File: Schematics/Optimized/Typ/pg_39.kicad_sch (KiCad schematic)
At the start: 35 parts, among them U4101 F374, U4102 F00, U4103 F04, U4104 F30, U4105 F51, U4109 F37, U4110 F02, U4111 F64, U4112 F64, U4113 F02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

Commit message: TYP+VAL condensation
Tested: passed expmon_test_val (-muxbus)
Tested: passed expmon_test_typ (-muxbus)
Tested: passed run_udiag
Tested: passed boot_env (R2_INTEG until PRETTY_PRINTER)
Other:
- moved on the sheet: GB226, GB274, GB275, GB276, GB277, GB278, GB281, GB282, GB283, GB284, U4104, U4105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

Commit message: Integrate R2_TV (mainly state clock)
Tested: passed run_udiag
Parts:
- removed U4105: F51, symbol r1000:F51
- removed U4109, U4124, U4125, U4126: F37, symbol r1000:F37
- removed U4119: F00, symbol r1000:F00
- removed U4121, U4122, U4123: F02, symbol r1000:F02
- added GB301, GB302, GB303, GB304, GB305, GB308, GB309, GB310, GB311, GB312, GB313, GB314: GB, symbol r1000:GB
- added U2117: XTVSCLK, symbol r1000:XTVSCLK
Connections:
- net ARF_WE.EN~: now also U2117.23 (ARFWR)
- net BRF_WE.EN~: now also U2117.26 (BRFWR)
- net CLK.2XE~: now also GB302.1
- net COND_CLK.EN~: now also U2117.11 (CCE)
- net COND~.SCLK: now also U2117.4 (CCLK)
- net CSA.DIAG.EN~: now also U2117.13 (ACE)
- net CSA~.SCLK: now also U2117.6 (ACLK)
- net H1: now also GB309.1
- net H2: now also GB310.1, U2117.3 (H2)
- net H2E: now also GB308.1
- net OF_CLK.EN~: now also U2117.9 (ZCE)
- net OF~.SCLK: now also U2117.2 (ZCLK)
- net Q2~: now also GB312.1
- net Q3~: now also GB313.1, U2117.5 (Q3)
- net RAM_STOP~: now also U2117.20 (RMS)
- net SF_STOP: now also U2117.18 (SFS)
- net STATE_CLK.EN~: now also U2117.7 (SCE)
- net STATE_STOP~: now also U2117.19 (STS)
- net UIR.DIAG_OFF: now also U2117.17 (UOF)
- net UIR.DIAG_ON~: now also U2117.15 (UON)
- net UIR~.SCLK: now also U2117.8 (UCLK)
- net WE.EN~: now also U2117.22 (WEEN)
- net WEL: now reaches U4117.5 (D3), U4118.5 (Q)
- net WEL: now also U2117.21 (WEL)
- new net ACS.DIAG_OFF~: U2117.24 (ACOFF)
- new net A_L.DIAG_OFF~: U2117.25 (ALOFF)
- new net A_RF.CS~: U2117.10 (ARFCS)
- new net A_RF.WE~: U2117.12 (ARFWE)
- new net BCS.DIAG_OFF~: U2117.27 (BCOFF)
- new net B_L.DIAG_OFF~: U2117.28 (BLOFF)
- new net B_RF.CS~: U2117.14 (BRFCS)
- new net B_RF.WE~: U2117.16 (BRFWE)
- new net CLK.2X: GB303.1
- new net CLK.2XE: GB301.1, U2117.1 (2XE)
- new net CLK.2X~: GB304.1
- new net H1.PHD: GB305.1
- new net Q1~: GB311.1
- new net Q4~: GB314.1
- no-connect marks 13 -> 11
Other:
- moved on the sheet: GB226, GB274, GB275, GB276, GB277, GB278, GB281, GB282, GB283, GB284, GB285, GB291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

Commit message: XCLKSTP, XIOP XSUDEC
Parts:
- removed GB308: GB, symbol r1000:GB
- removed U4102: F00, symbol r1000:F00
- removed U4103, U4114, U4115, U4116: F04, symbol r1000:F04
- removed U4104: F30, symbol r1000:F30
- removed U4110, U4113: F02, symbol r1000:F02
- removed U4111, U4112: F64, symbol r1000:F64
- added U901: F04, symbol r1000:F04
- added U903: XCLKSTPTV, symbol r1000:XCLKSTPTV
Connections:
- net WE.EN~ is gone; now on net DIAG_STOP: U2117.22 (DSTOP)
- net DIAG.NO_STOP: now also U903.3 (DFCLK)
- net DIAG_STOP: now also U4118.2 (D)
- net FREEZE: now also U903.6 (FREEZ)
- net Q3~: now also U903.1 (Q3)
- net Q4~: now also U901.1 (D0)
- net RAM_STOP~: now also U903.8 (RAMRUN)
- net SF_STOP: now also U903.4 (SFSTP)
- net STATE_STOP~: now also U903.2 (CLKRUN)
- net T.BHMAC_STOP~: now also U903.18 (STOP7)
- net T.DIAG_FREEZE~: now also U903.7 (DIAG1); no longer U4101.14 (D5)
- net T.DIAG_SYNC~: now also U903.5 (DIAG0); no longer U4101.13 (D4)
- net T.ECC_STOP: now also U903.9 (ECC0)
- net T.ECC_STOP.EN: now also U903.10 (ECC1)
- net T.FIELD_STOP~: now also U903.16 (STOP5)
- net T.MEM_STOP~: now also U903.11 (STOP0)
- net T.MICRO_STOP~: now also U903.17 (STOP6)
- net T.SPARE_STOP~: now also U903.13 (STOP2)
- net T.SYS_STOP~: now also U903.12 (STOP1)
- net T.TYPE0_STOP~: now also U903.14 (STOP3)
- net T.TYPE1_STOP~: now also U903.15 (STOP4)
- net WEL: now also U4118.6 (Q_); no longer U4118.5 (Q)
- net H2E: no longer names the net of U4117.1 (D0)
- net H2E: now also U901.2 (Q)
- new net CSA_WRITE_EN: U903.19 (CSAWR)
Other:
- moved on the sheet: GB226, GB274, GB275, GB276, GB277, GB278, GB281, GB282, GB283, GB284, GB285, GB291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

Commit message: Lots of work
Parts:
- removed GB311: GB, symbol r1000:GB
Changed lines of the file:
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@@
-    (stroke (width 0) (type default))
-  )
-  (wire (pts (xy 205.74 15.24) (xy 210.82 15.24))
     (stroke (width 0) (type default))
   )
@@
     (effects (font (size 2.54 2.54)) (justify left))
     (property "Intersheetrefs" "${INTERSHEET_REFS}" (at 542.5803 81.1213 0)
-      (effects (font (size 1.905 1.905)) (justify left))
-    )
-  )
-  (global_label "Q1~" (shape output) (at 210.82 15.24 0) (fields_autoplaced)
-    (effects (font (size 2.54 2.54)) (justify left))
-    (property "Intersheetrefs" "${INTERSHEET_REFS}" (at 223.2072 15.24 0)
       (effects (font (size 1.905 1.905)) (justify left))
     )
@@
         )
       )
-    )
-  )
-  (symbol (lib_id "r1000:GB") (at 205.74 15.24 0) (mirror y) (unit 1)
-    (in_bom yes) (on_board yes) (dnp no)
-    (property "Reference" "GB311" (at 201.93 15.24 0)
-      (effects (font (size 2.54 2.54)) (justify left))
-    )
-    (property "Value" "GB" (at 205.74 15.24 0)
-      (effects (font (size 1.27 1.27)) hide)
-    )
-    (property "Footprint" "" (at 205.74 15.24 0)
-      (effects (font (size 1.27 1.27)) hide)
-    )
-    (property "Datasheet" "" (at 205.74 15.24 0)
-      (effects (font (size 1.27 1.27)) hide)
-    )
-    (pin "1")
-    (instances
-      (project "TYP"
-        (path "/20011966-7b12-533f-4d20-457d979e0ec9/20011966-0ba5-12d7-17ec-25639cf29a65"
-          (reference "GB311") (unit 1)
-        )
-      )

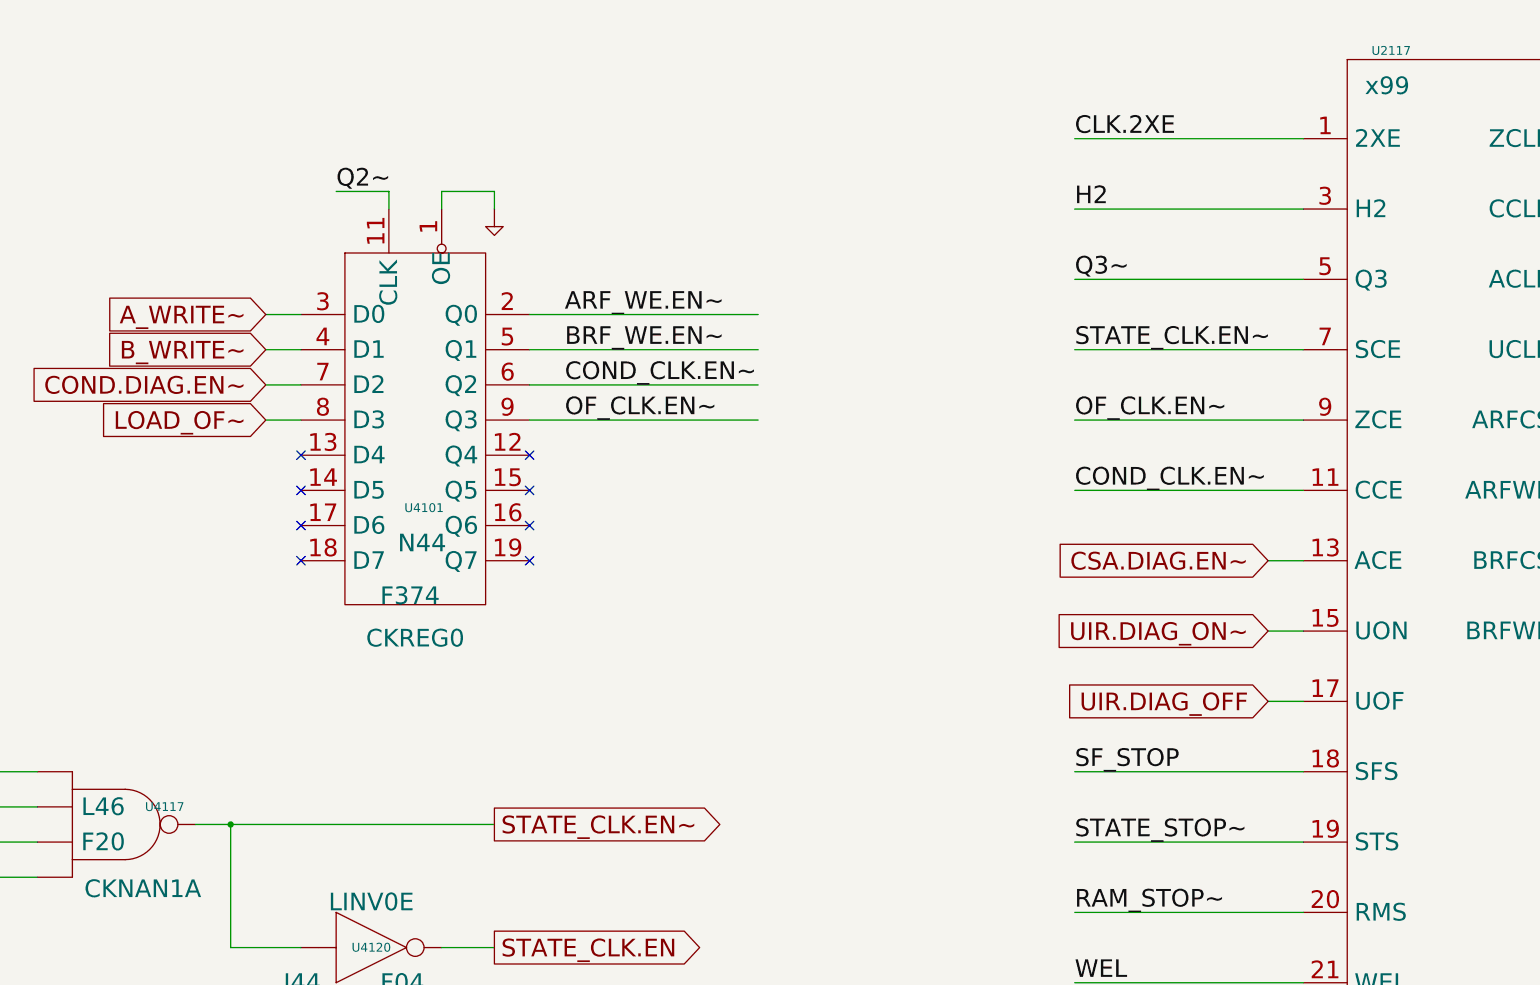
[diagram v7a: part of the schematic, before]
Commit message: Update to kicad9
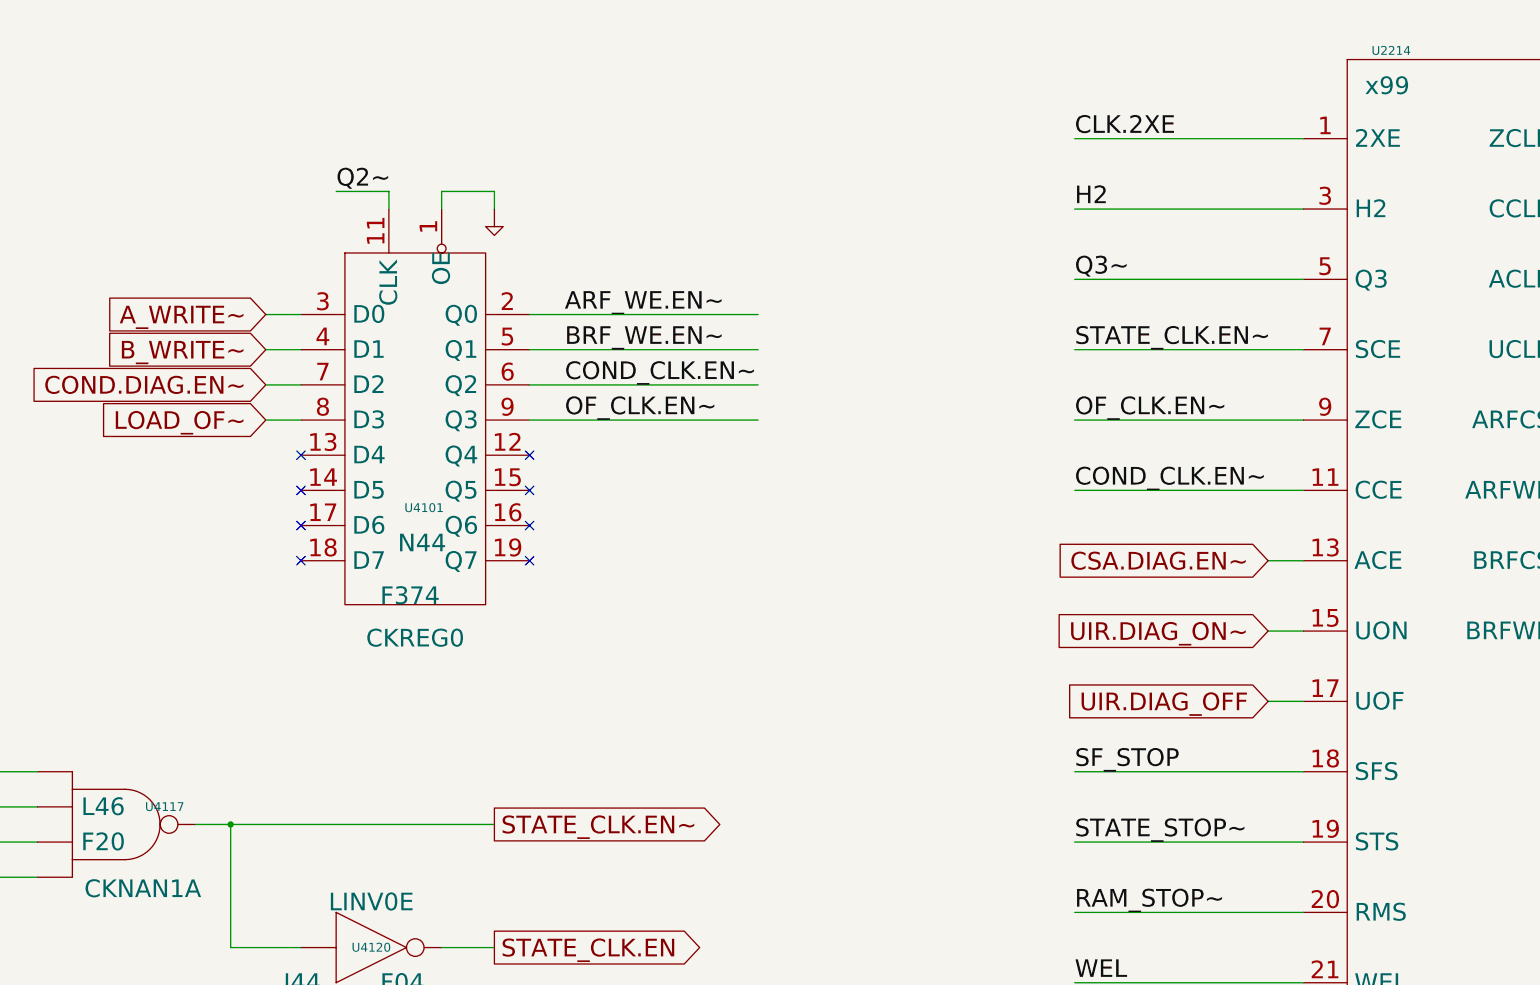
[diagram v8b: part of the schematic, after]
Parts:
- renumbered U2117 to U2214
